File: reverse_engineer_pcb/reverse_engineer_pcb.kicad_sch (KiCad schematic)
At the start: 68 parts, among them IC3 CD4051B, IC4 CD4051B, IC5 CD4051B, IC8 CD4051B, IC9 CD4051B, X0 TestPoint, X1 TestPoint, X10 TestPoint, X11 TestPoint, X12 TestPoint, X13 TestPoint, X14 TestPoint, X15 TestPoint, X16 TestPoint, X17 TestPoint, X18 TestPoint, X19 TestPoint, X2 TestPoint, X3 TestPoint, X4 TestPoint, X5 TestPoint, X6 TestPoint, X7 TestPoint, X8 TestPoint, X9 TestPoint, Y0 TestPoint, Y1 TestPoint, Y10 TestPoint, Y11 TestPoint, Y12 TestPoint, Y2 TestPoint, Y3 TestPoint, Y4 TestPoint, Y5 TestPoint, Y6 TestPoint, Y7 TestPoint, Y8 TestPoint, Y9 TestPoint

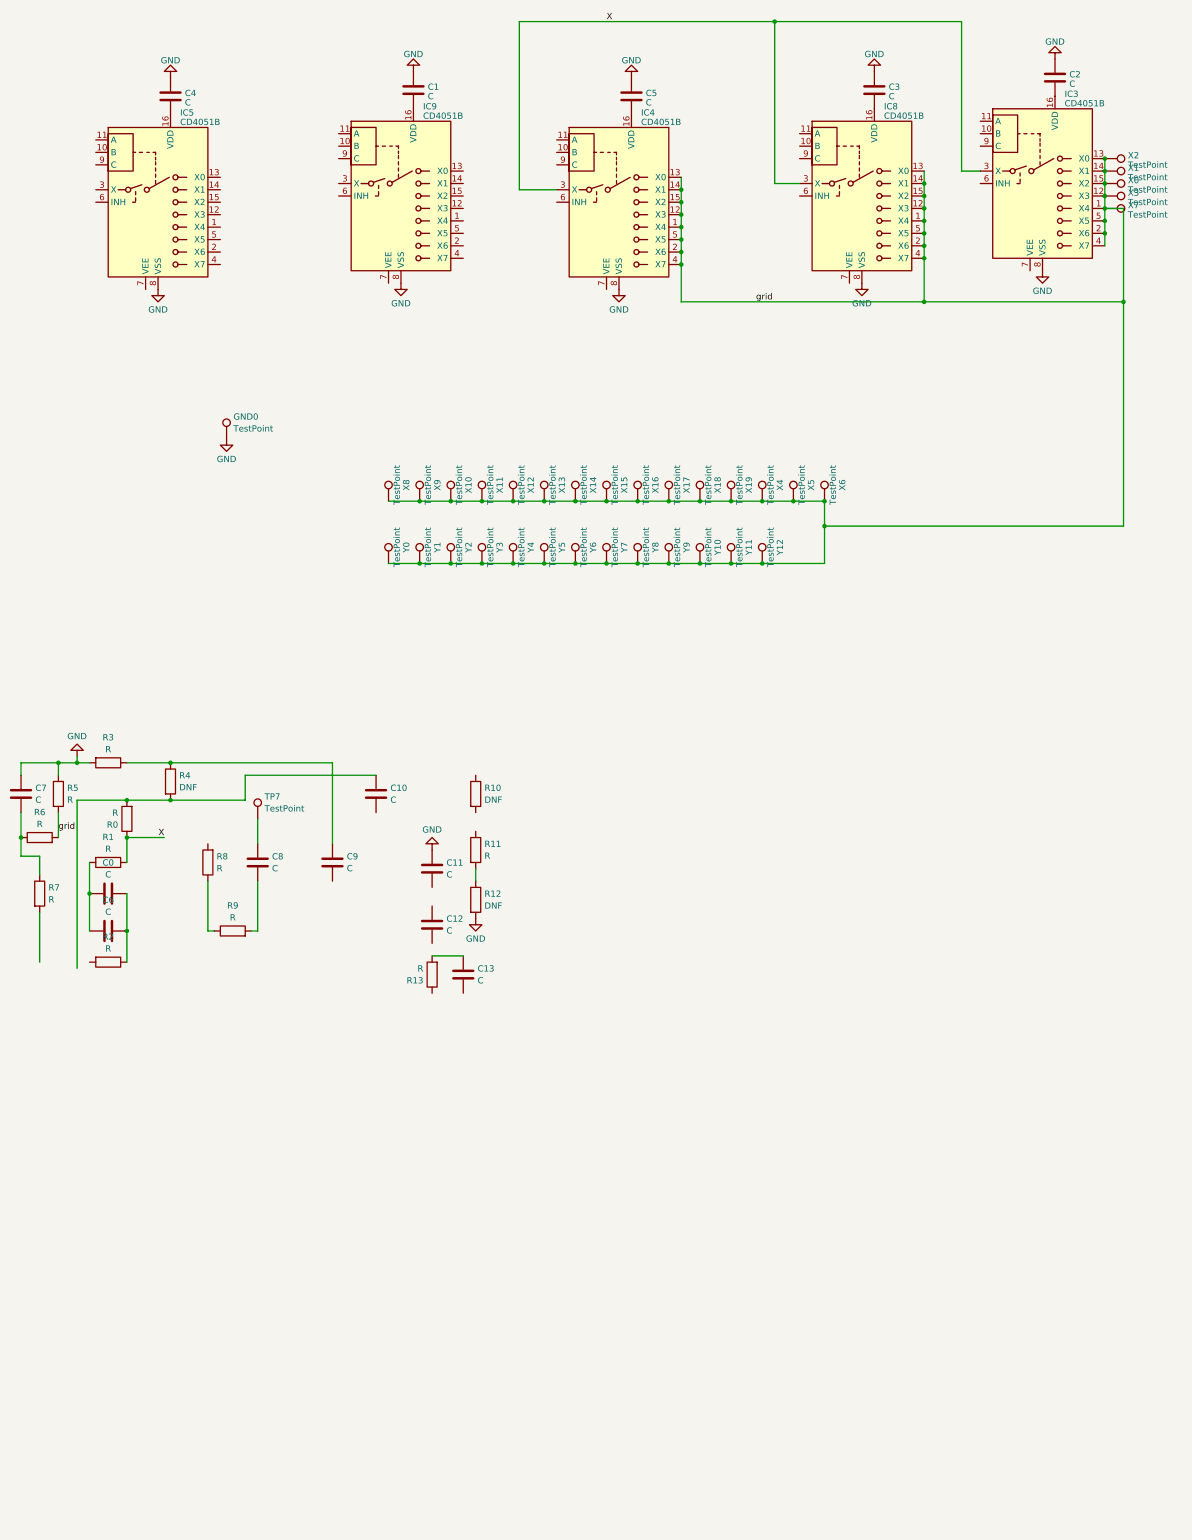
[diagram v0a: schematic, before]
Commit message: Traced most of pcb, if I haven't forgotten anything, the grid should be fully traced
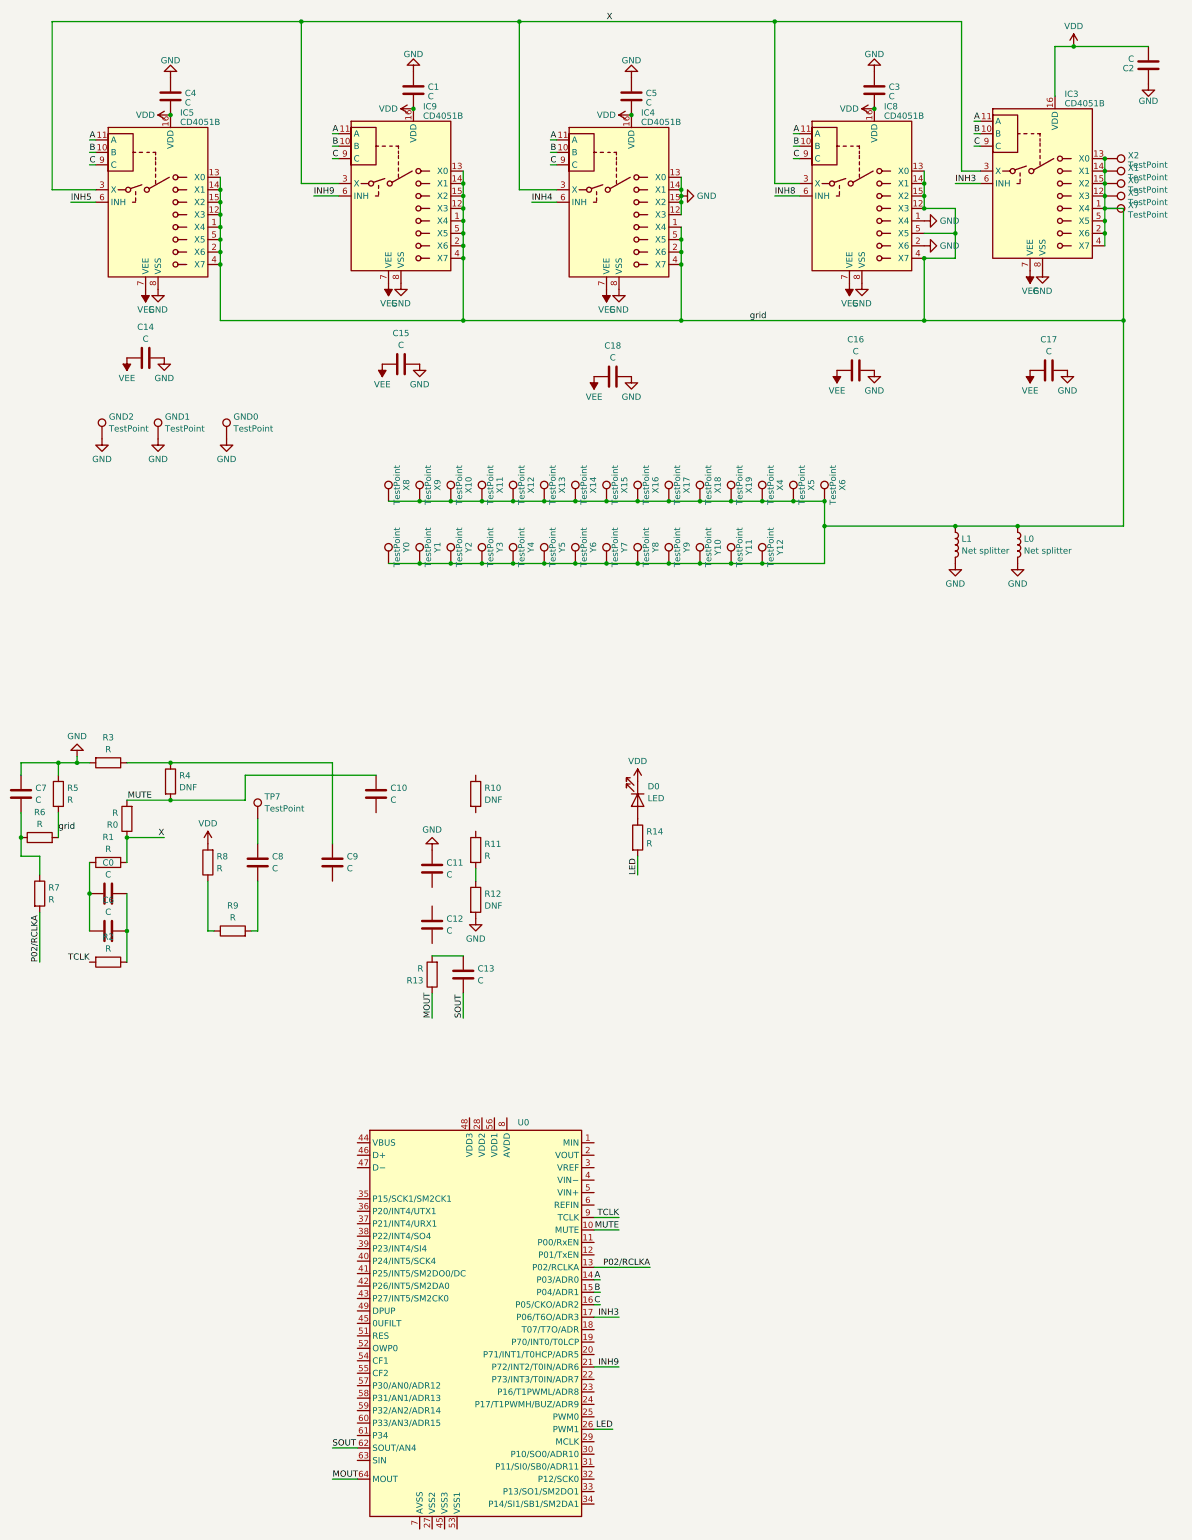
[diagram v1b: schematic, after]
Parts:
- added C14, C15, C16, C17, C18: C, Capacitor_SMD:C_0402_1005Metric, symbol Device:C
- added D0: LED, LED_SMD:LED_0603_1608Metric, symbol Device:LED
- added GND1, GND2: TestPoint, TestPoint:TestPoint_Pad_D1.0mm, symbol Connector:TestPoint
- added L0, L1: Net splitter, local:net splitter .4mm, symbol Device:L
- added R14: R, Resistor_SMD:R_0402_1005Metric, symbol Device:R
- added U0: ~, Package_QFP:TQFP-64_7x7mm_P0.4mm, symbol local:LC87F9W48A
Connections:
- net GND: now also IC4.12 (X3), IC4.13 (X0), IC4.14 (X1), IC4.15 (X2), IC8.1 (X4), IC8.2 (X6), C14.2, C15.2, C16.2, C17.2, C18.2, GND1.1, GND2.1, L0.2, L1.2
- net X: now also IC5.3 (X), IC9.3 (X)
- net grid: now also IC5.1 (X4), IC5.12 (X3), IC5.13 (X0), IC5.14 (X1), IC5.15 (X2), IC5.2 (X6), IC5.4 (X7), IC5.5 (X5), IC9.1 (X4), IC9.12 (X3), IC9.13 (X0), IC9.14 (X1), IC9.15 (X2), IC9.2 (X6), IC9.4 (X7), IC9.5 (X5), L0.1, L1.1; no longer IC4.12 (X3), IC4.13 (X0), IC4.14 (X1), IC4.15 (X2), IC8.1 (X4), IC8.2 (X6)
- net SOUT: now reaches C13.2
- net SOUT: now also U0.62 (SOUT/AN4)
- net MUTE: now reaches C10.1, R0.2, R4.2
- net MUTE: now also U0.10 (MUTE)
- net VDD: now reaches C1.2, IC9.16 (VDD)
- net VDD: now also C2.2, C3.2, C4.2, C5.2, IC3.16 (VDD), IC4.16 (VDD), IC5.16 (VDD), IC8.16 (VDD), R8.2, D0.1 (K)
- net MOUT: now reaches R13.1
- net MOUT: now also U0.64 (MOUT)
- net B: now reaches IC9.10 (B)
- net B: now also IC3.10 (B), IC4.10 (B), IC5.10 (B), IC8.10 (B), U0.15 (P04/ADR1)
- net A: now reaches IC9.11 (A)
- net A: now also IC3.11 (A), IC4.11 (A), IC5.11 (A), IC8.11 (A), U0.14 (P03/ADR0)
- net INH9: now reaches IC9.6 (INH)
- net INH9: now also U0.21 (P72/INT2/T0IN/ADR6)
- net VEE: now reaches IC9.7 (VEE)
- net VEE: now also IC3.7 (VEE), IC4.7 (VEE), IC5.7 (VEE), IC8.7 (VEE), C14.1, C15.1, C16.1, C17.1, C18.1
- net C: now reaches IC9.9 (C)
- net C: now also IC3.9 (C), IC4.9 (C), IC5.9 (C), IC8.9 (C), U0.16 (P05/CKO/ADR2)
- net INH5: now reaches IC5.6 (INH)
- net TCLK: now reaches R2.2
- net TCLK: now also U0.9 (TCLK)
- net P02/RCLKA: now reaches R7.2
- net P02/RCLKA: now also U0.13 (P02/RCLKA)
- net INH3: now reaches IC3.6 (INH)
- net INH3: now also U0.17 (P06/T6O/ADR3)
- net INH4: now reaches IC4.6 (INH)
- net INH8: now reaches IC8.6 (INH)
- new net: D0.2 (A), R14.1
- new net LED: R14.2, U0.26 (PWM1)
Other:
- moved on the sheet: C2

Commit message: Finish tracing entire pcb
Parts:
- added C19, C20, C21, C22, C23: C, Capacitor_SMD:C_0603_1608Metric, symbol Device:C
- added C24, C25, C26, C27, C28, C30, C32: C, Capacitor_SMD:C_0402_1005Metric, symbol Device:C
- added C29, C31: C, Capacitor_SMD:C_0805_2012Metric, symbol Device:C
- added D1: DNF, Diode_SMD:D_0603_1608Metric, symbol Device:D
- added D2: D, Diode_SMD:D_SOD-123, symbol Device:D
- added D3, D4: D, Diode_SMD:D_SOD-523, symbol Device:D
- added L2: L, Inductor_SMD:L_0603_1608Metric, symbol Device:L
- added L3: L_Ferrite, Resistor_SMD:R_0603_1608Metric, symbol Device:L_Ferrite
- added Q0: Q_NPN_BEC, Package_TO_SOT_SMD:SOT-323_SC-70, symbol Device:Q_NPN_BEC
- added R15: DNF, Resistor_SMD:R_0402_1005Metric, symbol Device:R
- added R16, R17, R18, R19, R20, R21, R22, R23: R, Resistor_SMD:R_0402_1005Metric, symbol Device:R
- added R24: 0, Resistor_SMD:R_0603_1608Metric, symbol Device:R
- added TP11, TP13, TP14, TVEE: TestPoint, TestPoint:TestPoint_Pad_D1.0mm, symbol Connector:TestPoint
- added Y13: Crystal_GND24, Crystal:Crystal_SMD_2520-4Pin_2.5x2.0mm, symbol Device:Crystal_GND23
- R8, R9: footprint Resistor_SMD:R_0603_1608Metric -> Resistor_SMD:R_0402_1005Metric
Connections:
- net GND: now also C8.2, R10.1, U0.27 (VSS2), U0.45 (VSS3), U0.53 (VSS1), U0.7 (AVSS), C19.2, C20.1, C21.1, C22.1, C23.1, C25.1, C26.1, C27.2, C28.2, C29.2, C30.1, C31.2, C32.1, D2.2 (A), D3.1 (K), R18.1, R19.1, Y13.2, Y13.3
- net INH4: now also U0.18 (T07/T7O/ADR)
- net INH5: now also U0.20 (P71/INT1/T0HCP/ADR5)
- net INH8: now also U0.22 (P73/INT3/T0IN/ADR7)
- net VDD: now also R11.1, R8.1, U0.28 (VDD2), U0.56 (VDD1), C21.2, C22.2, D1.1 (K), L2.1, Q0.2 (E), R15.2, R18.2, R22.1, TP11.1; no longer R8.2
- net VEE: now also C32.2, D4.2 (A), TVEE.1
- net grid: no longer IC8.4 (X7), R5.2, R6.2
- net REFIN: now reaches C8.1, TP7.1
- net REFIN: now also U0.6 (REFIN)
- net P34: now reaches R11.2, R12.1
- net P34: now also U0.61 (P34)
- net SIN: now reaches C13.1, R13.2
- net SIN: now also U0.63 (SIN)
- net VIN+: now reaches C9.2
- net VIN+: now also U0.5 (VIN+)
- net VIN-: now reaches C10.2
- net VIN-: now also U0.4 (VIN−)
- net at C12.1: now also U0.1 (MIN)
- net at C12.2: now also U0.2 (VOUT)
- net at R9.1: now also C26.2, Y13.4; no longer R8.1
- net CF2: now reaches R9.2
- net CF2: now also U0.55 (CF2); no longer C8.2
- net P30: now reaches R10.2
- net P30: now also U0.57 (P30/AN0/ADR12)
- net MCLK: now reaches U0.29 (MCLK)
- net MCLK: now also C24.1
- net VREF: now reaches U0.3 (VREF)
- net VREF: now also C11.2
- net at U0.44 (VBUS): now also R8.2, C23.2
- net D+: now reaches U0.46 (D+)
- net D+: now also C27.1, R16.1
- net D-: now reaches U0.47 (D−)
- net D-: now also C28.1, R17.1
- net at U0.48 (VDD3): now also C20.2, R15.1
- net DPUP: now reaches U0.49 (DPUP)
- net DPUP: now also R21.2
- net RES: now reaches U0.51 (RES)
- net RES: now also C30.2, D1.2 (A), R22.2, TP13.1
- net OWP0: now reaches U0.52 (OWP0)
- net OWP0: now also R19.2, TP14.1
- net CF1: now reaches U0.54 (CF1)
- net CF1: now also C25.2, Y13.1
- net at U0.8 (AVDD): now also C19.1, L2.2
- new net: D2.1 (K), L3.1, R24.2
- new net: C31.1, Q0.1 (B), R23.1
- new net: C24.2, D3.2 (A), D4.1 (K)
- new net: C29.1, R20.1
- new net: Q0.3 (C), R23.2, R24.1
- new net ?1: IC8.4 (X7), R5.2, R6.2
- new net D+_: R16.2, R21.1
- new net D-_: R17.2
- new net UFILT: R20.2, U0.50 (UFILT)
- new net VBUS: L3.2
- no-connect marks 0 -> 23
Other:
- note added: "Capacitance multiplier"
- note added: "Negative voltage generator"
- moved on the sheet: C0, C10, C11, C12, C13, C2, C3, C6, C7, C8, C9, D0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

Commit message: Add block diagram symbol
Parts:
- added unit 2 of U0
- C21: PIN (none) -> 56
- C22: PIN (none) -> 28
- L4: renamed from R1; value R -> L; symbol Device:R -> Device:L
- renumbered TVEE to TVEE0
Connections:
- net GND: now also U0.7 (AVSS); no longer U0.53 (VSS1), U0.7 (AVSS)
- net MOUT: now also U0.64; no longer U0.64 (MOUT)
- net REFIN: now also U0.6; no longer U0.6 (REFIN)
- net SIN: now also U0.63; no longer U0.63 (SIN)
- net SOUT: now also U0.62; no longer U0.62 (SOUT/AN4)
- net VIN+: now also U0.5; no longer U0.5 (VIN+)
- net VIN-: now also U0.4; no longer U0.4 (VIN−)
- net VREF: now also U0.3; no longer U0.3 (VREF)
- net µVBUS: now reaches C23.2, R8.2, U0.44 (VBUS)
- net VDD3: now reaches C20.2, R15.1, U0.48 (VDD3)
- net at C12.1: now also U0.1; no longer U0.1 (MIN)
- net at C12.2: now also U0.2; no longer U0.2 (VOUT)
- net at C6.1, R2.1: now also C0.2; no longer C0.1
- net AVDD: now reaches C19.1, L2.2
- net AVDD: now also U0.8 (AVDD); no longer U0.8 (AVDD)
- net at C6.2, L4.2: now also C0.1; no longer C0.2
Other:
- note removed: "Capacitance multiplier"
- note removed: "Negative voltage generator"
- moved on the sheet: C0, C1, C10, C11, C12, C13, C14, C15, C16, C17, C18, C19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

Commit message: add some clarity and info to pcb and schematic
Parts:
- R10, R12, R15, R4: now not fitted
- R2: value R -> 120
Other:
- note added: "8.14nF combined"
- note added: "GRID"
- moved on the sheet: C0, C6, L4, R2
